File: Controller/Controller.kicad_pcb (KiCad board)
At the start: 4 copper layers, 75 x 57 mm, 63 parts, among them CN1 SERVO_PWM, CN10 FEMALE_LEFT, CN11 FEMALE_RIGHT, CN2 CFG1, CN3 CFG1, CN4 CFG1, CN5 FEMALE_LEFT, CN6 FEMALE_RIGHT, CN7 CFG1, CN8 CFG1, CN9 CFG1, J1 PJ-202AH, J10 ICSP, J11 MotorTerm, J12 MotorHeader, J13 MotorTerm, J14 MotorHeader, J15 12V_TERM, J2 TermLaser, J3 TermStop, J4 LASER_PWR, J5 LASER_PULSE, J6 TermControl, J7 TermLimit, J8 TermAux, J9 UJ2-BH-1-TH, K1 SW_RESET, U1 CJ7805, U2 INTERFACE-CH340T_SSOP20_, U3 MCU-ATMEGA328P-AU_TQFP32_, Y1 12MHz, Y2 16MHZ

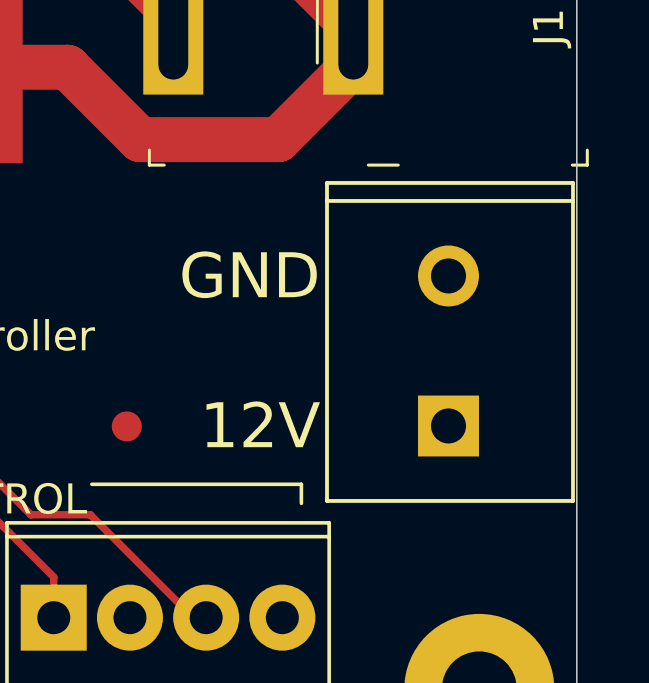
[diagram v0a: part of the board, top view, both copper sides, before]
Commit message: Finished adding 3D models
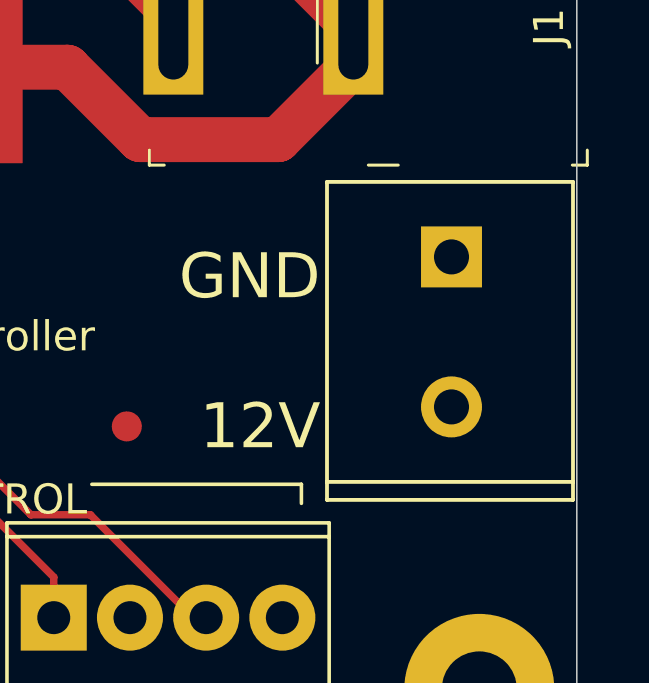
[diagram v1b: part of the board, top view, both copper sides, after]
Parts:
- moved J15 0.64 mm to (215.8, 69.8), turned to 270 degrees
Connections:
- J15 pad 1: /VIN_12V -> GND
- J15 pad 2: GND -> /VIN_12V
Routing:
- net /VIN_12V: track 152.1 -> 149.8 mm
- net GND: track 543.5 -> 542.9 mm

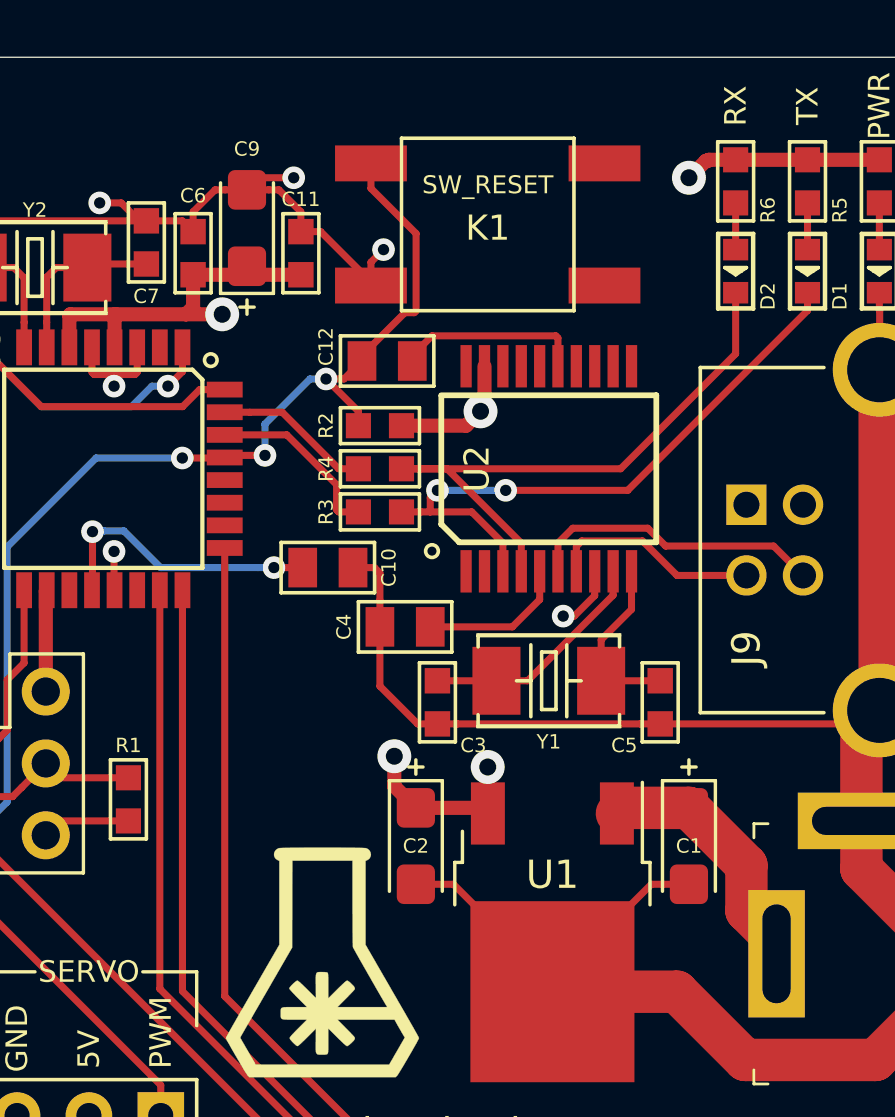
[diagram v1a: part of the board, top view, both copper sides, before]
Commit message: Fixing 10uF caps
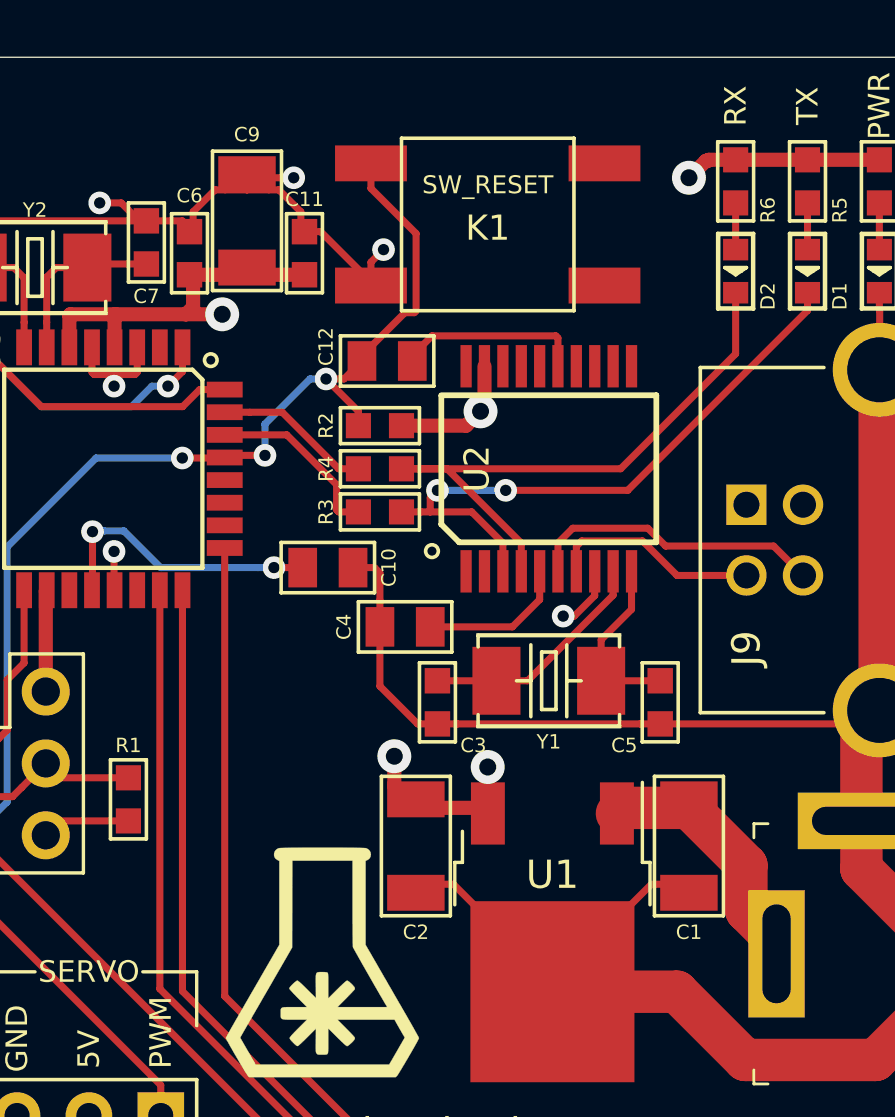
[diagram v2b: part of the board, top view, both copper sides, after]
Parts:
- C1, C2, C9: footprint Capacitor_Tantalum_SMD:CP_EIA-3216-18_Kemet-A -> OPL_Capacitor:C1206
- moved C9 0.25 mm to (187.8, 33.8)
- moved C11 0.13 mm to (189.9, 34.9)
- moved C6 0.13 mm to (185.8, 34.9)
